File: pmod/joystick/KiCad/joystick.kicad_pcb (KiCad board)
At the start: 2 copper layers, 37 x 33 mm, 7 parts, among them J1 Conn_01x06_Pin, U1 COM-09032

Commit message: fix: Pridal jsem opravy, ktere byly navrzene
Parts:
- added H3: MountingHole, MountingHole:MountingHole_3.2mm_M3_DIN965, F.Cu at (97.2, 37.4)
- added H4: MountingHole, MountingHole:MountingHole_3.2mm_M3_DIN965, F.Cu at (97.2, 62.4)
- moved H2 1.00 mm to (67.2, 62.4)
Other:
- board text added: "25mm"
- board text added: "30mm"

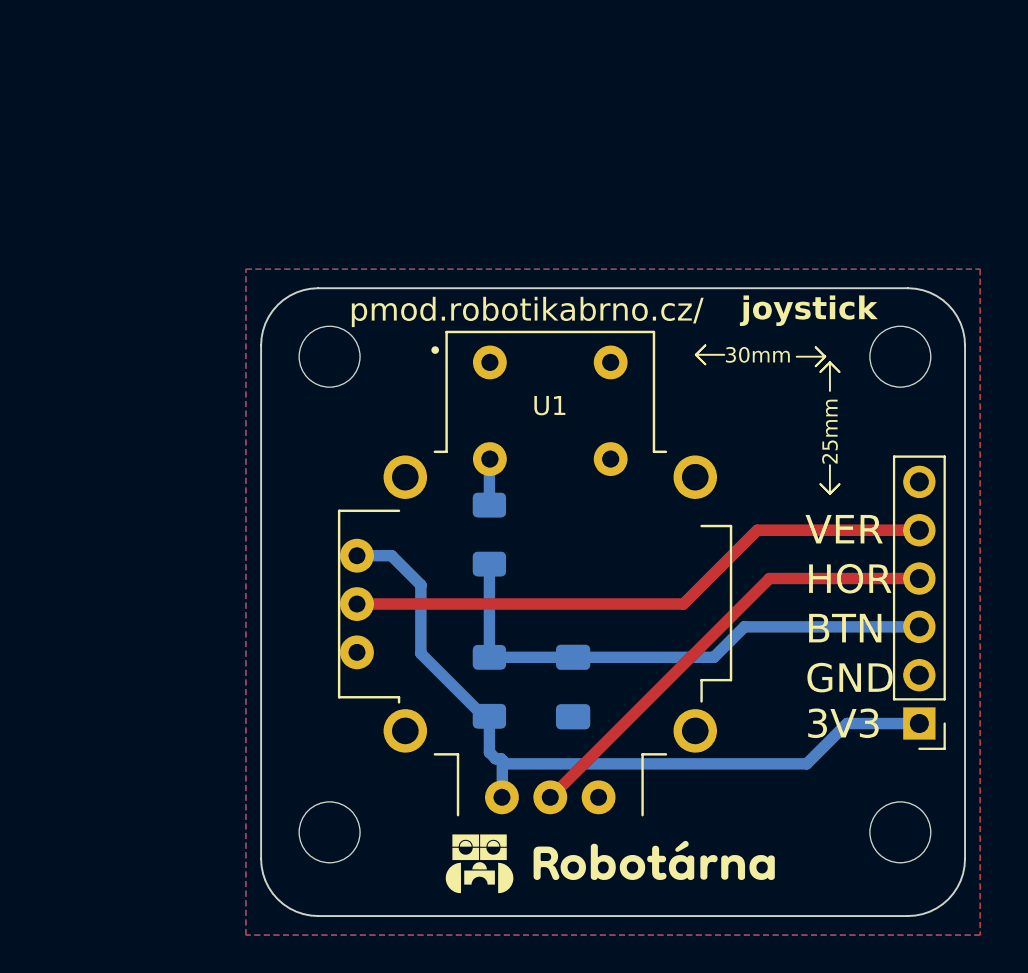
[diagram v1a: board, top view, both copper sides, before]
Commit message: fix: prepare all board for manufacturing
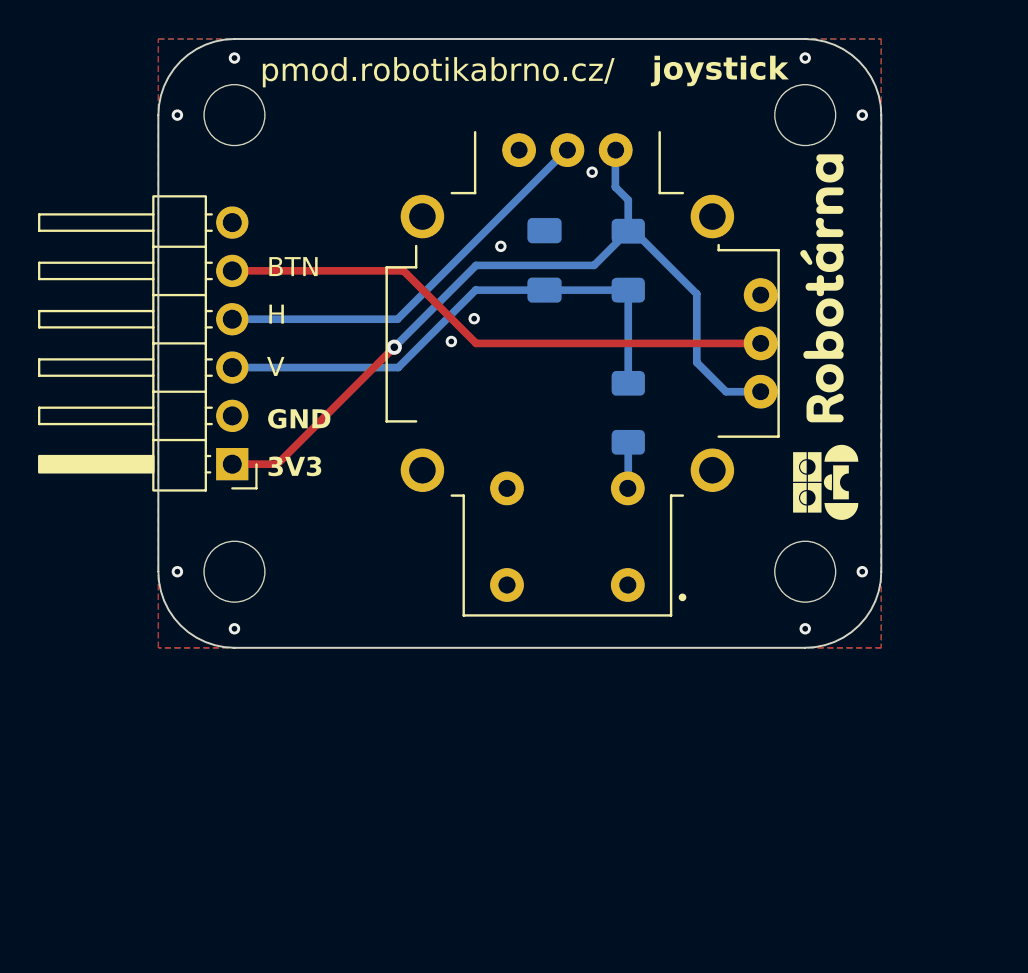
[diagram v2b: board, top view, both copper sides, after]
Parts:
- H1, H2, H3, H4: footprint MountingHole:MountingHole_3.2mm_M3_DIN965 -> MountingHole:MountingHole_3.2mm_M3
- J1: footprint Connector_PinHeader_2.54mm:PinHeader_1x06_P2.54mm_Vertical -> Connector_PinHeader_2.54mm:PinHeader_1x06_P2.54mm_Horizontal
- moved H4 51.4 mm to (62.2, 24.7), turned to 180 degrees
- moved H2 45.2 mm to (92.2, 24.7), turned to 180 degrees
- moved J1 38.6 mm to (62.1, 43.0)
- moved H3 36.8 mm to (62.2, 48.7), turned to 180 degrees
- moved H1 27.4 mm to (92.2, 48.7), turned to 180 degrees
- moved R1 23.6 mm to (82.9, 32.4), turned to 90 degrees
- moved C1 22.5 mm to (78.5, 32.3), turned to 90 degrees
- moved U1 13.7 mm to (79.7, 36.7), turned to 180 degrees
- moved R2 9.71 mm to (82.9, 40.4), turned to -90 degrees
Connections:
- C1 pad 1: /SEL -> /V
- J1 pad 3: /SEL -> /V
- J1 pad 5: /V -> /SEL
- R1 pad 1: /SEL -> /V
- R2 pad 1: /SEL -> /V
- U1 pad V2: /V -> /SEL
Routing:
- net /V: track 31.1 -> 27.4 mm
- net /H: track 24.1 -> 21.3 mm
- net /3V3: track 40.2 -> 43.0 mm, vias 0 -> 1
- net /SEL: track 28.2 -> 29.3 mm
- net /GND: vias 0 -> 12
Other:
- board size 37 x 33 mm -> 38 x 32 mm
- board text added: "32mm"
- board text added: "38mm"
- board text added: "H"
- board text added: "V"
- board text removed: "25mm"
- board text removed: "30mm"
- board text removed: "HOR"
- board text removed: "VER"
